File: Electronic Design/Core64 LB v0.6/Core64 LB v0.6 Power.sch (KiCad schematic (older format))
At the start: 26 parts, among them IC1 LP3961EMP-5.0, IC2 TPS7A0533PDBVR, J3 Conn_01x08_Female, J7 S03B-PASK-2_LF__SN_, J8 5V0 Cur. Mon., J9 3V3 Cur. Mon., Q1 MCC_SL3401A, SW1 JS102011SAQN, U6 Micro_LiPo_Charger

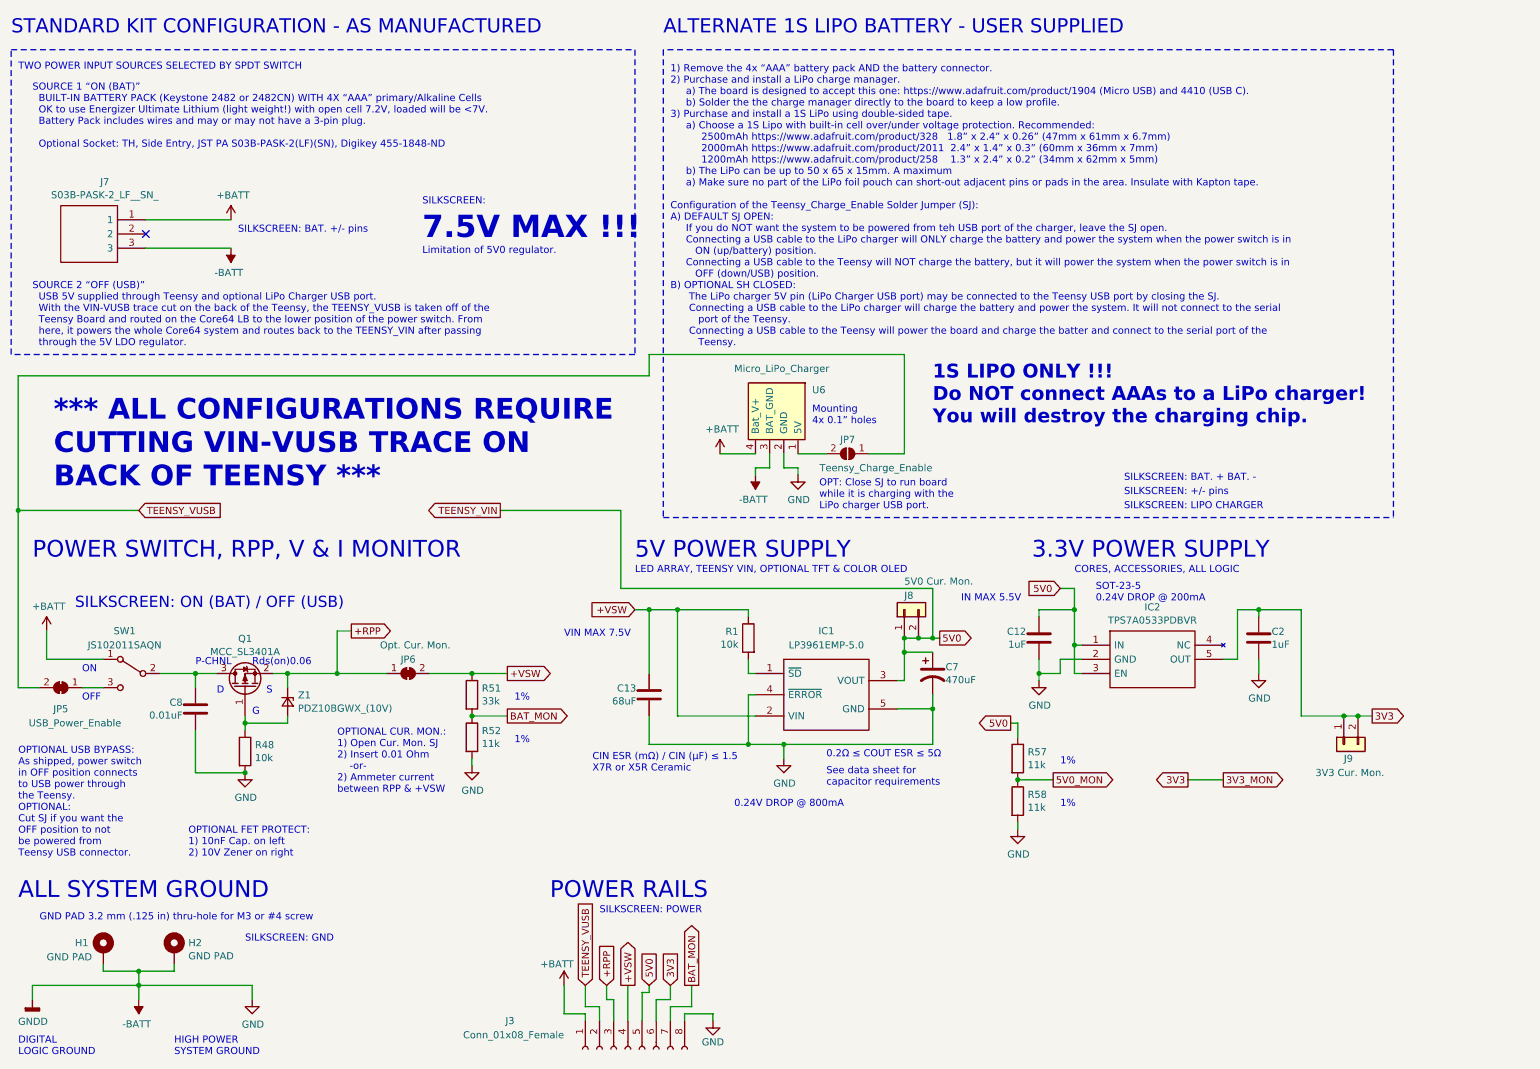
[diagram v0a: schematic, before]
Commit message: APPLY LOGIC BOARD V0.5 FIXES NEEDED TO BE V0.6 U1 silk screen should be placed by pin 1 not pin 7 Check J1 and J2 labels so J1 is on the left, like it is for the Core Board Remove Header for old LED Matrix, since is no longer needed and it is in the way. RTC Notes on schematic, must add THREE things, typo change from TWO. Below JP5 Teensy Charge Enable is a rogue "+" on the silk screen Left of R56 is a dead-end trace stub. Doesn't hurt anything but it's not right. 6.8 Ohm Core Current Limit Resistors can move to 5%. JP1/2 for OLED should be JP1/2 on the OLED silk screen, not JP3/4 Silk screen, left header row, swap SEN1 and SEN2 text so they match to S1 and S2 correctly on the inner perimeter. Move to larger logo and other text on the backside Update silk screen for all boards with P/Ns, bare board. Move top row of TFT LCD support down 0.55mm. Add 470 resistor to gate of core array enable to limit current. Change I2C pull-up resistors from 2.2K to 1.2K 20% (E12 series is most common, and values overlap) Remove two dead-end GND (BAT-) traces between/below Teensy 25/26, and over to QWIIC. Add I2C series resistors 68 Ohm at output of Teensy. Move the 470uF LED 5V0 capacitor, down to be between 5V0 Cur Mon and Teensy Charge enable jumpers, out of the way of the batteries. New stylus position is on left, so the 3V3 capacitor needs to move in a few mm to allow it to pass through. Provide thru-holes for alternate 3.3V and 5V bulk capacitor options. Propagation through sense logic chips was 200ns, reduce PU to 1K2 and remove inline 10Ks. Now 50ns. Voltage divider and other resistors, consolidated to 10K resistors. Keep the two 10K resistors on the 5V0 MON. Add a SJ in series to isolate from Hall Switches. Replace the inline 10K resistors in the all optional Voltage Monitoring lines with closed SJs instead. Clean-up all the horz/vert traces left from removing LED drive header and relocating the driver and 5V0 cap Part substitutions Data sheet updates
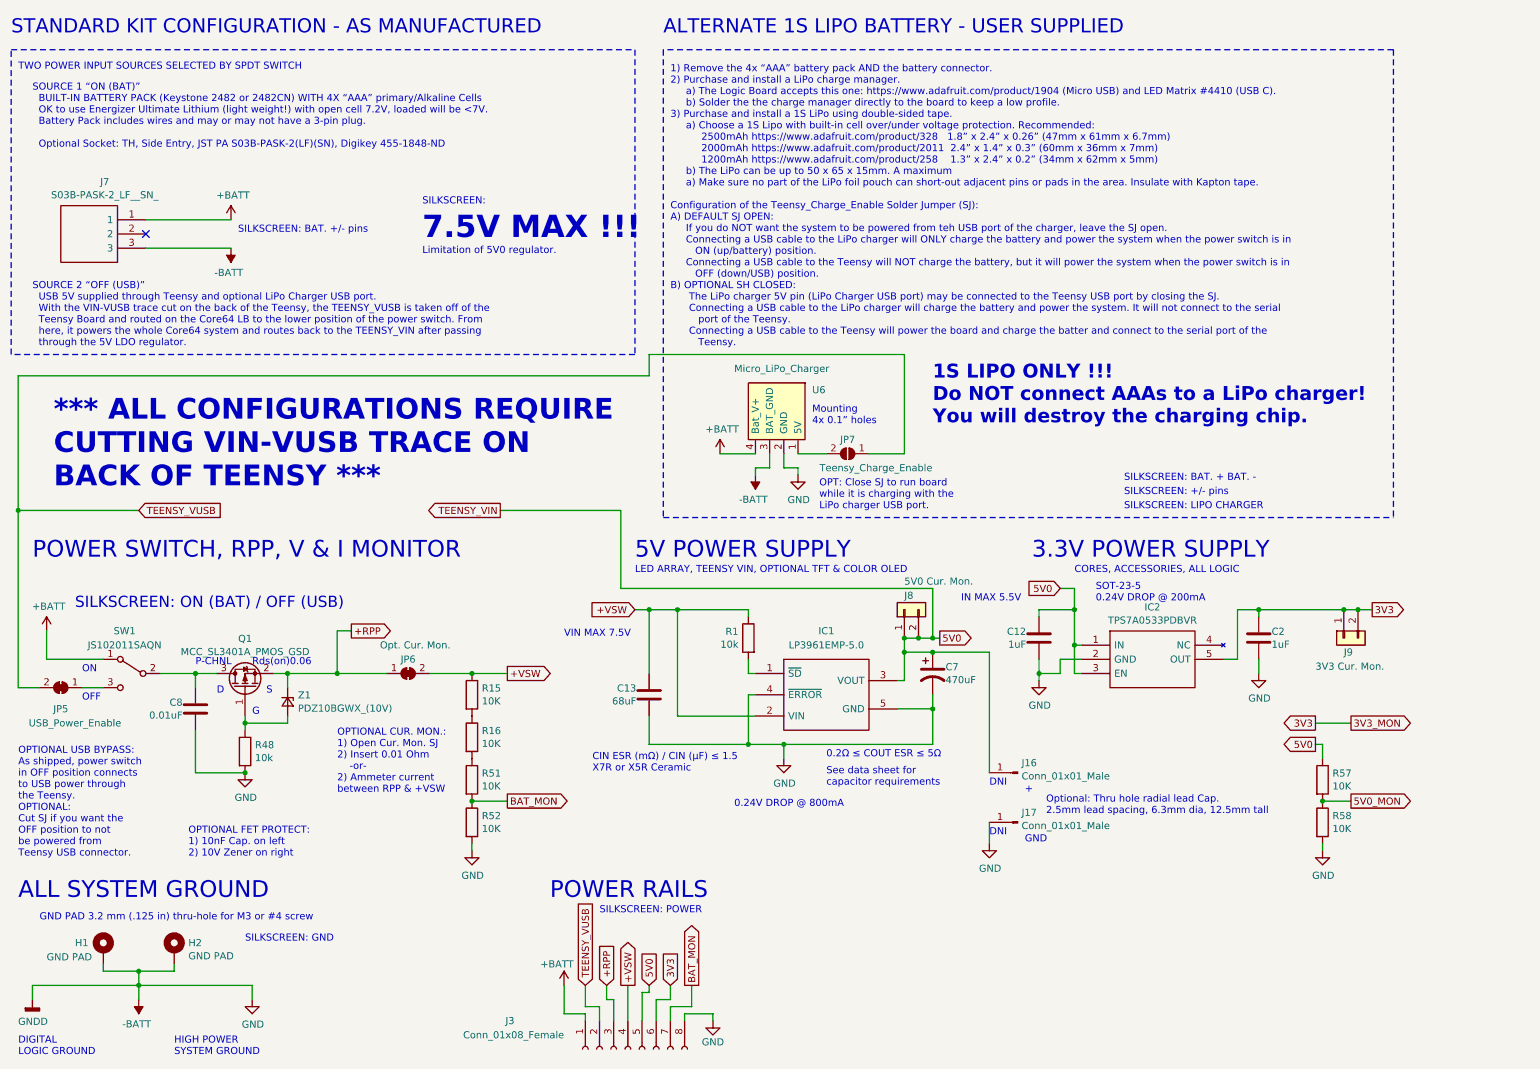
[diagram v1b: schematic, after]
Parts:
- added J16, J17: Conn_01x01_Male, Connector_PinHeader_2.54mm:PinHeader_1x01_P2.54mm_Vertical_No_Registration, symbol Connector:Conn_01x01_Male
- added R15, R16: 10K, Resistor_SMD:R_0805_2012Metric, symbol Device:R
- IC1: MPN (none) -> LP3961EMP-5.0/NOPB
- IC2: MPN (none) -> TPS7A0533PDBVR
- Q1: value MCC_SL3401A -> MCC_SL3401A_PMOS_GSD; Description (none) -> MOSFET P-CHNL GSD LOW RDS(ON); MPN (none) -> SL3401A-TP; MPN(Secondary) (none) -> DMP3125L-7; Manufacturer(Secondary) (none) -> Diodes Inc.; Manufacturer_Name (none) -> Micro Commercial Co
- R51: value 33k -> 10K
- R52, R57, R58: value 11k -> 10K
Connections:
- net +VSW: now also R15.1; no longer R51.1
- net -BATT: now also J17.1 (Pin_1)
- net 5V0: now also J16.1 (Pin_1)
- new net: R16.2, R51.1
- new net: R15.2, R16.1
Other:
- note added: "+"
- note added: "1) Remove the 4x “AAA” battery pack AND the battery connector.\n2) Purchase and install a LiPo charge manager.\n a) The Logic Board accepts this one: https://www.adafruit.com/product/1904 (Micro USB) and LED Matrix #4410 (USB C).\n b) Solder the the charge manager directly to the board to keep a low profile.\n3) Purchase and install a 1S LiPo using double-sided tape. \n a) Choose a 1S Lipo with b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"
- note added: "DNI"
- note added: "GND"
- note added: "Optional: Thru hole radial lead Cap.\n2.5mm lead spacing, 6.3mm dia, 12.5mm tall"
- note removed: "1%"
- note removed: "1) Remove the 4x “AAA” battery pack AND the battery connector.\n2) Purchase and install a LiPo charge manager.\n a) The board is designed to accept this one: https://www.adafruit.com/product/1904 (Micro USB) and 4410 (USB C).\n b) Solder the the charge manager directly to the board to keep a low profile.\n3) Purchase and install a 1S LiPo using double-sided tape. \n a) Choose a 1S Lipo with built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"
- moved on the sheet: J9, R51, R52, R57, R58

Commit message: Revise LB V0.6, part substitutions, data sheet updates, clean up Ref. Des. to be in order and easier to find on the board in groups
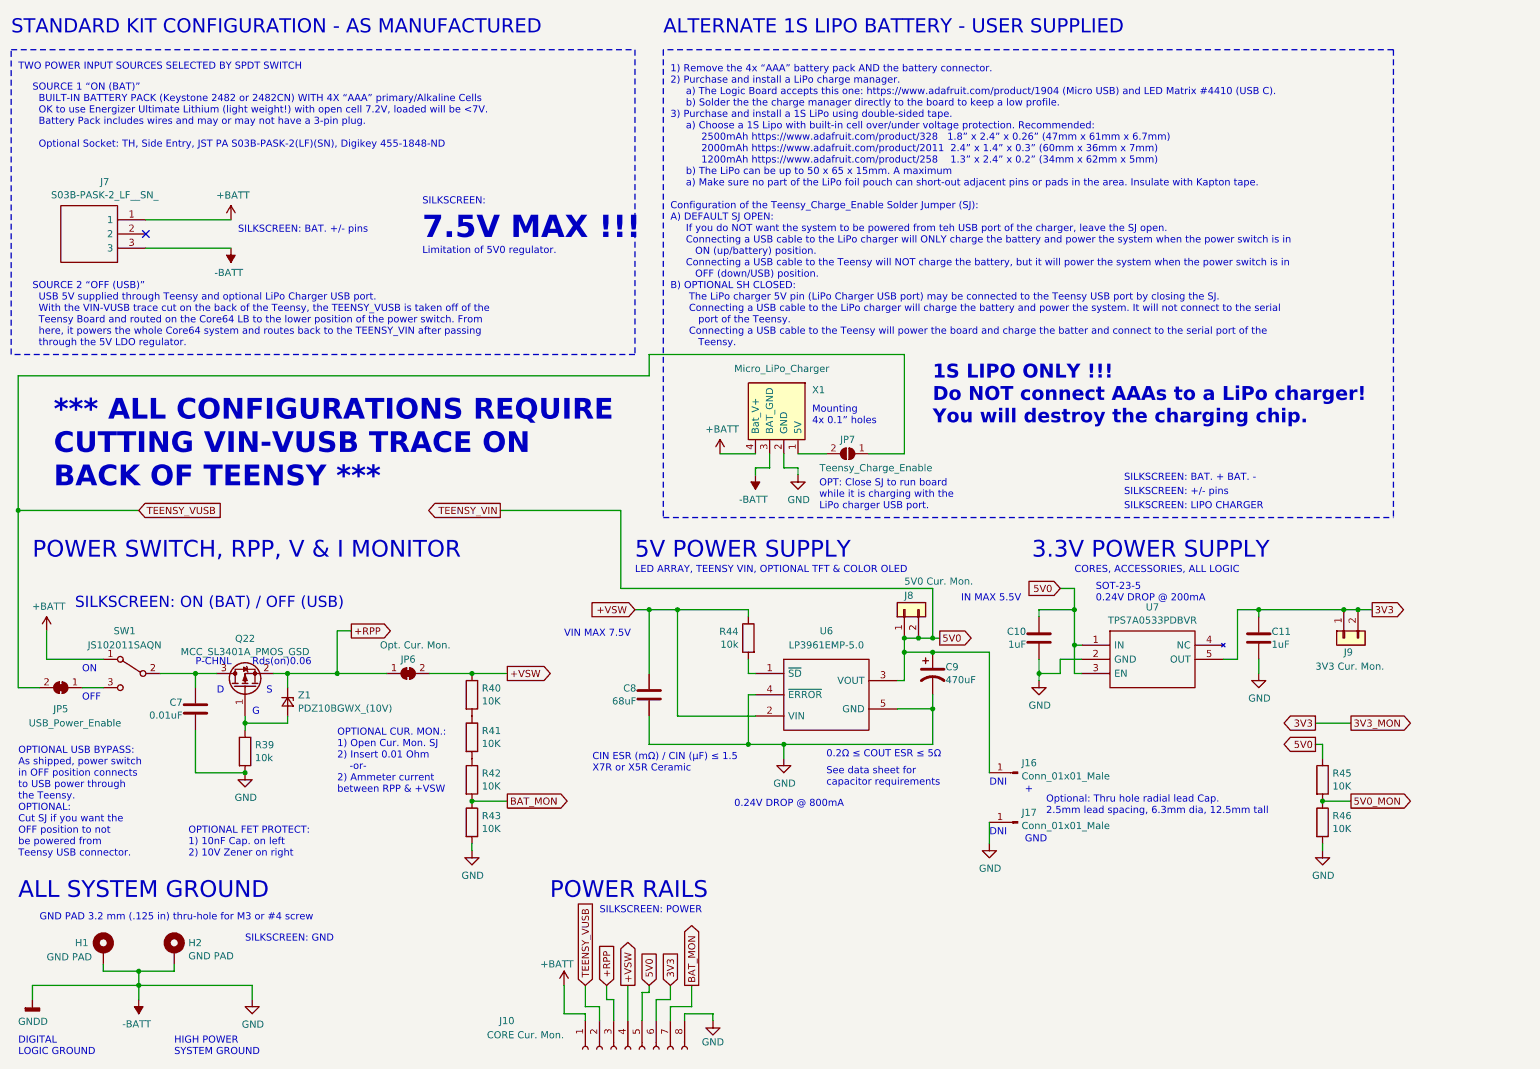
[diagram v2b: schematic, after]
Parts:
- C10: renamed from C12; Description (none) -> CAP; Insert? (none) -> Yes
- C11: renamed from C2; Description (none) -> CAP; Insert? (none) -> Yes
- C7: renamed from C8; Description (none) -> CAP; Insert? (none) -> No
- C8: renamed from C13; Description (none) -> CAP; Insert? (none) -> Yes
- C9: renamed from C7; Description (none) -> CAP ALUM 470UF 20% 10V SMD; Insert? (none) -> Yes; MPN(Secondary) (none) -> 6.3SEV330M6.3X8; Manufacturer(Secondary) (none) -> Rubycon; Value_Modifier (none) -> 330UF 20% 6.3V
- H1, H2, J16, J17, J7, J8, JP5, JP6, JP7: Insert? (none) -> No
- J10: renamed from J3; value Conn_01x08_Female -> CORE Cur. Mon.; Insert? (none) -> No
- J9: Insert? (none) -> No; MPN (none) -> SN74HC02DR
- Q22: renamed from Q1; Insert? (none) -> Yes
- R39: renamed from R48; Description (none) -> RES 10K OHM; Insert? (none) -> Yes; Value_Modifier (none) -> 20%
- R40: renamed from R15; Description (none) -> RES 10K OHM; Insert? (none) -> Yes; Value_Modifier (none) -> 20%
- R41: renamed from R16; Description (none) -> RES 10K OHM; Insert? (none) -> Yes; Value_Modifier (none) -> 20%
- R42: renamed from R51; Description (none) -> RES 10K OHM; Insert? (none) -> Yes; Value_Modifier (none) -> 20%
- R43: renamed from R52; Description (none) -> RES 10K OHM; Insert? (none) -> Yes; Value_Modifier (none) -> 20%
- R44: renamed from R1; Description (none) -> RES 10K OHM; Insert? (none) -> Yes; Value_Modifier (none) -> 20%
- R45: renamed from R57; Description (none) -> RES 10K OHM; Insert? (none) -> Yes; Value_Modifier (none) -> 20%
- R46: renamed from R58; Description (none) -> RES 10K OHM; Insert? (none) -> Yes; Value_Modifier (none) -> 20%
- SW1: Description (none) -> SWITCH SLIDE SPDT 300MA 6V; Insert? (none) -> Yes; MPN (none) -> JS102011SAQN; Manufacturer_Name (none) -> C&K
- U6: renamed from IC1; Insert? (none) -> Yes Yes
- U7: renamed from IC2; Description 1-A, ultra-low-IQ, 200-mA low-dropout (LDO) regulator in a 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 -> Linear Voltage Regulator IC Positive Fixed 1 Output 200mA S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; Insert? (none) -> Yes; MPN(Secondary) (none) -> TPS7A0533PDBVT; Manufacturer(Secondary) (none) -> Texas Instruments
- X1: renamed from U6; Description (none) -> LIPO CHARGE MODULE; Insert? (none) -> No
- Z1: Description (none) -> DIODE, ZENER; Insert? (none) -> No
